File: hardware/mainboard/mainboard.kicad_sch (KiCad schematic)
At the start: 1 part, among them J1 EXT

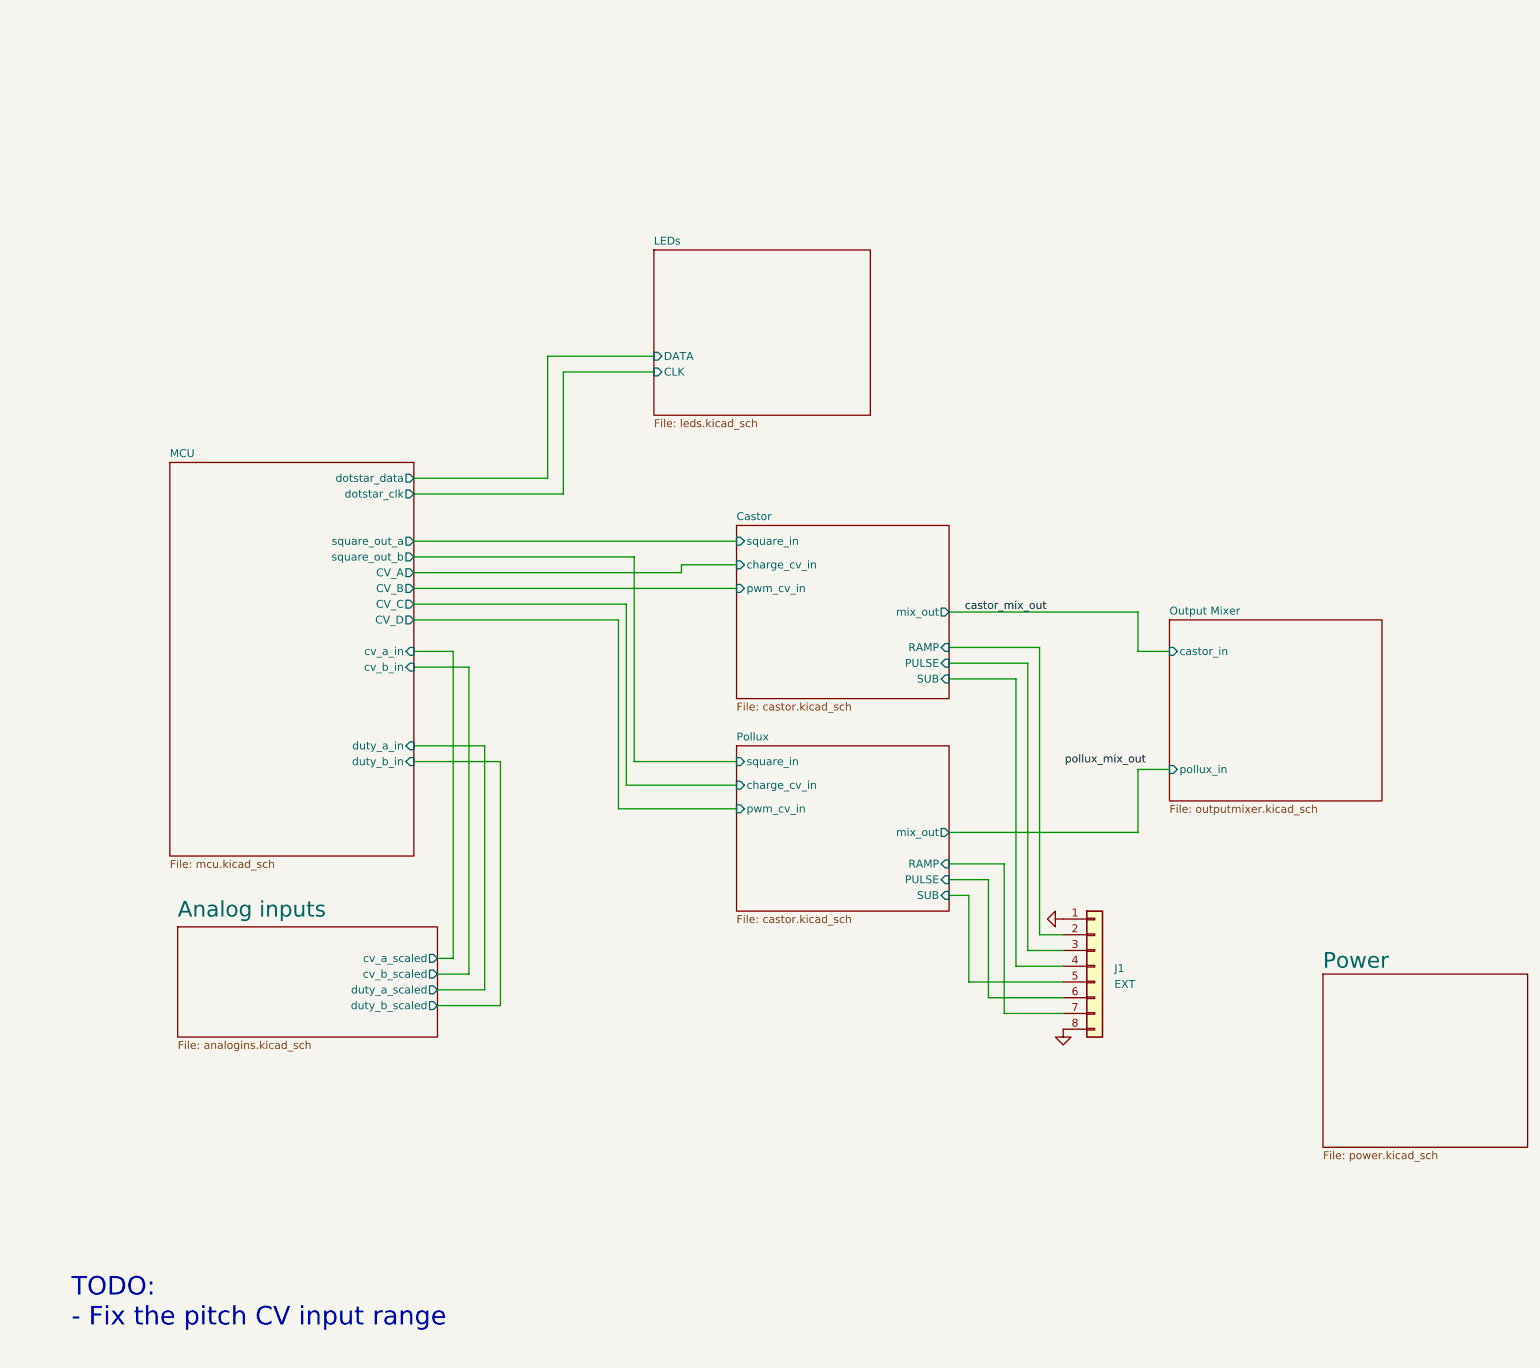
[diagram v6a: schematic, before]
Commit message: Cleanup MCU schematic
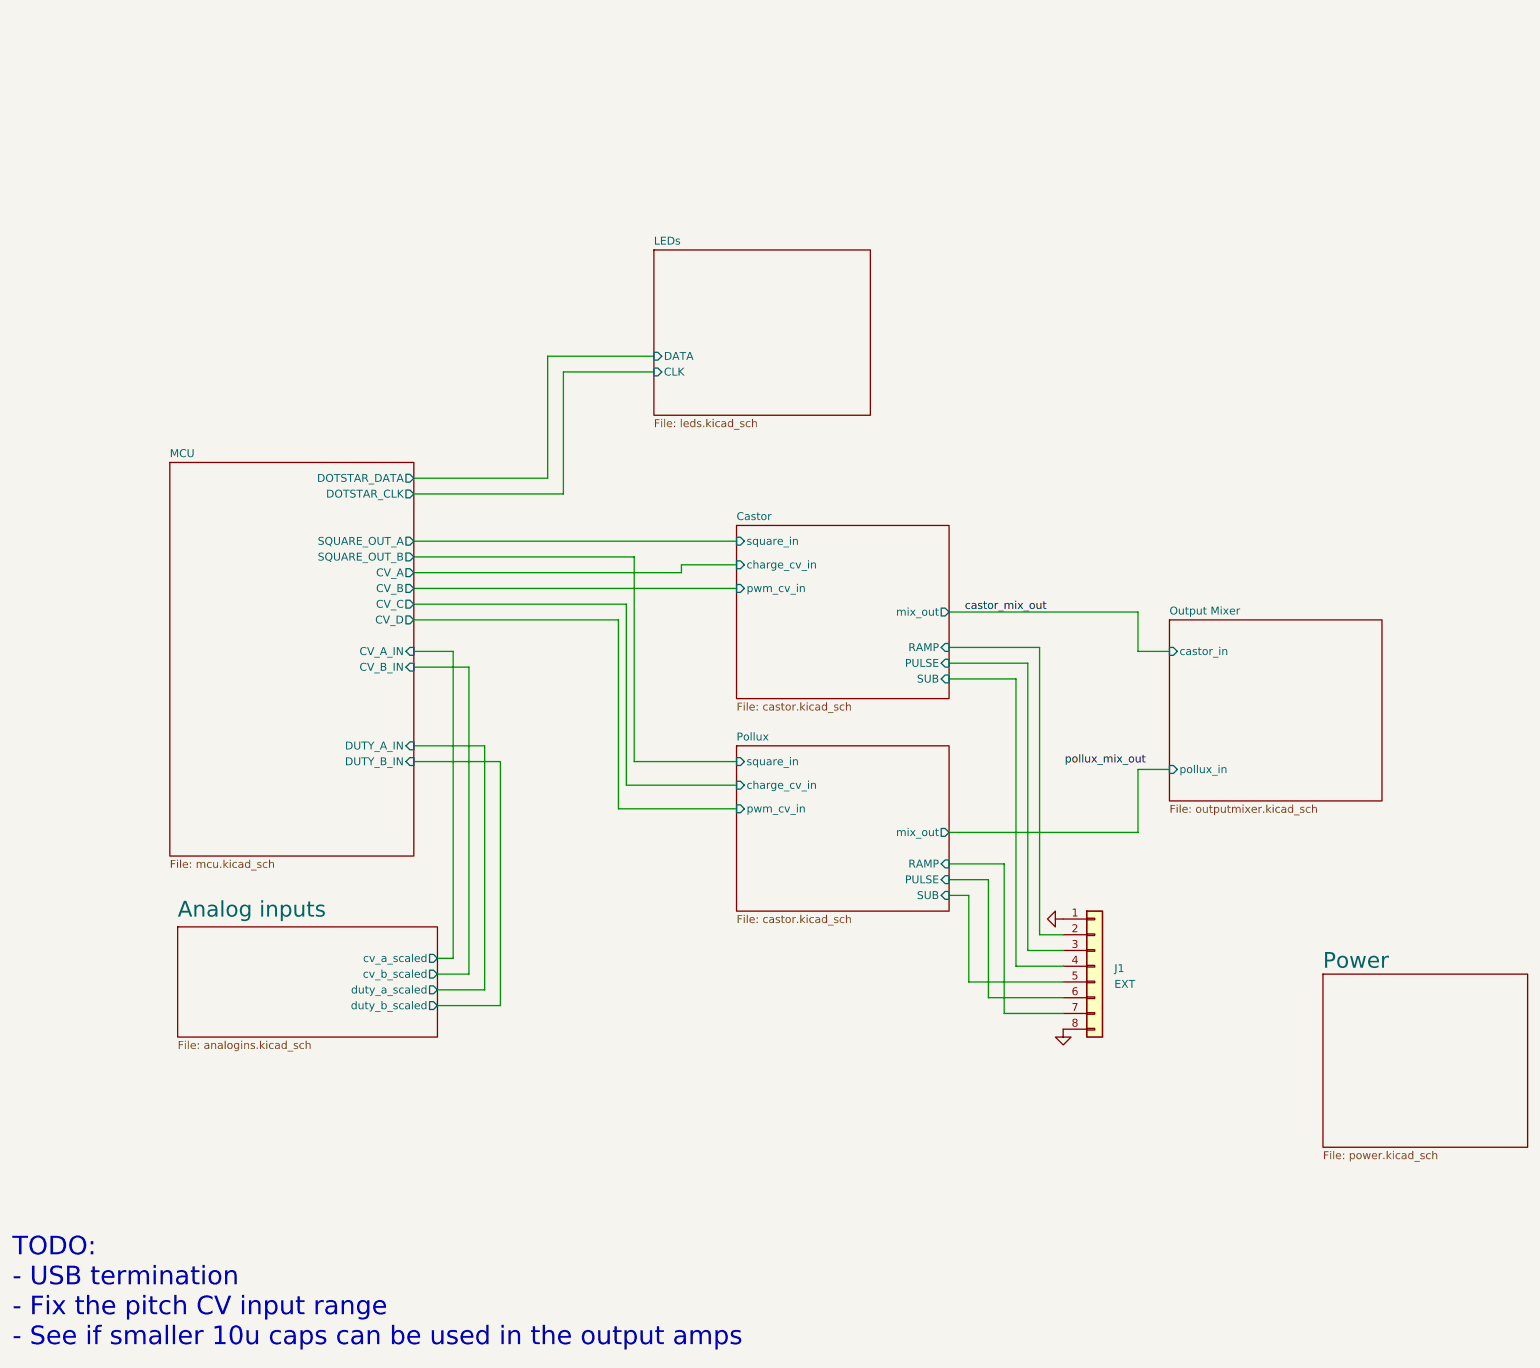
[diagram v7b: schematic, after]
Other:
- sheet MCU ports: added CV_A_IN, CV_B_IN, DOTSTAR_CLK, DOTSTAR_DATA, DUTY_A_IN, DUTY_B_IN, SQUARE_OUT_A, SQUARE_OUT_B; removed cv_a_in, cv_b_in, dotstar_clk, dotstar_data, duty_a_in, duty_b_in, square_out_a, square_out_b
- note added: "TODO: - USB termination - Fix the pitch CV input range - See if smaller 10u caps can be used in the output amps"
- note removed: "TODO: - Fix the pitch CV input range"

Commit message: More schematic cleanup - nearly done!
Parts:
- removed J1: EXT, Connector_JST:JST_GH_BM08B-GHS-TBT_1x08-1MP_P1.25mm_Vertical, symbol Connector_Generic:Conn_01x08
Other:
- sheet Output Mixer renamed Mixer & outputs
- sheet Analog inputs ports: added CASTOR_DUTY_CV, CASTOR_PITCH_CV, POLLUX_DUTY_CV, POLLUX_PITCH_CV; removed cv_a_scaled, cv_b_scaled, duty_a_scaled, duty_b_scaled
- sheet Castor ports: added CHARGE_CV_IN, MIX_OUT, PULSE_OUT, PWM_CV_IN, RAMP_OUT, SQUARE_IN, SUB_OUT; removed PULSE, RAMP, SUB, charge_cv_in, mix_out, pwm_cv_in, square_in
- sheet MCU ports: added CASTOR_CHARGE_CV, CASTOR_DUTY_IN, CASTOR_PITCH_IN, CASTOR_PWM_CV, CASTOR_SQUARE_OUT, POLLUX_CHARGE_CV, POLLUX_DUTY_IN, POLLUX_PITCH_IN, POLLUX_PWM_CV, POLLUX_SQUARE_OUT; removed CV_A, CV_A_IN, CV_B, CV_B_IN, CV_C, CV_D, DUTY_A_IN, DUTY_B_IN, SQUARE_OUT_A, SQUARE_OUT_B
- sheet Mixer & outputs ports: added CASTOR_MIX_IN, CASTOR_PULSE_IN, CASTOR_RAMP_IN, CASTOR_SUB_IN, POLLUX_MIX_IN, POLLUX_PULSE_IN, POLLUX_RAMP_IN, POLLUX_SUB_IN; removed castor_in, pollux_in
- sheet Pollux ports: added CHARGE_CV_IN, MIX_OUT, PULSE_OUT, PWM_CV_IN, RAMP_OUT, SQUARE_IN, SUB_OUT; removed PULSE, RAMP, SUB, charge_cv_in, mix_out, pwm_cv_in, square_in
